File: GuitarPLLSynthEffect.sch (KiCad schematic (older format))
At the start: 36 parts

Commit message: Second draft PCB layout
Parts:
- C_PWRBY1: footprint Capacitors_SMD:C_0805_HandSoldering -> Capacitors_SMD:CP_Elec_4x5.3
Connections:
- net 9V: now also C_PWRBY1.1, C_PWRBY2.2
- net at D_IN1.2 (A), J_POWER1.2: no longer C_PWRBY1.1, C_PWRBY2.2
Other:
- moved on the sheet: C_PWRBY1, C_PWRBY2, D_IN1
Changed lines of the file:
@@
 	1    0    0    1
 $EndComp
-Text Label 2625 2100 3    60   ~ 0
+Text Label 3225 2100 3    60   ~ 0
 GND
 Text Label 4250 1400 0    60   ~ 0
@@
 Wire Wire Line
 	9950 5500 9950 5975
-Wire Wire Line
-	2050 1350 2050 1450
-Connection ~ 2050 1400
+Connection ~ 2650 1400
 Wire Wire Line
 	4075 1400 4075 1600
@@
 Optional clean signal for FX
 Wire Wire Line
-	1475 1400 3125 1400
-Wire Wire Line
-	3425 1400 5350 1400
+	2200 1400 5350 1400
 $Comp
 L _Schottky D_IN1
 U 1 1 5AC34A74
-P 3275 1400
-F 0 "D_IN1" H 3275 1500 50  0000 C CNN
-F 1 "_Schottky" H 3275 1300 50  0000 C CNN
-F 2 "Diodes_SMD:D_SOD-123F" H 3275 1400 50  0001 C CNN
-F 3 "" H 3275 1400 50  0001 C CNN
-	1    3275 1400
+P 2050 1400
+F 0 "D_IN1" H 2050 1500 50  0000 C CNN
+F 1 "_Schottky" H 2050 1300 50  0000 C CNN
+F 2 "Diodes_SMD:D_SOD-123F" H 2050 1400 50  0001 C CNN
+F 3 "" H 2050 1400 50  0001 C CNN
+	1    2050 1400
 	-1   0    0    1
 $EndComp
@@
 	1550 1600 1550 1825
 Wire Wire Line
-	1550 1825 2625 1825
-Wire Wire Line
-	2625 1750 2625 2100
-Wire Wire Line
-	2050 1750 2050 1825
-Connection ~ 2050 1825
+	1550 1825 3225 1825
+Wire Wire Line
+	3225 1750 3225 2100
+Wire Wire Line
+	2650 1750 2650 1825
+Connection ~ 2650 1825
 $Comp
 L C C_PWRBY1
 U 1 1 5AC36CD5
-P 2050 1600
-F 0 "C_PWRBY1" H 2075 1700 50  0000 L CNN
-F 1 "10uF" H 2075 1500 50  0000 L CNN
-F 2 "Capacitors_SMD:C_0805_HandSoldering" H 2088 1450 50  0001 C CNN
-F 3 "" H 2050 1600 50  0001 C CNN
-	1    2050 1600
+P 2650 1600
+F 0 "C_PWRBY1" H 2675 1700 50  0000 L CNN
+F 1 "10uF" H 2675 1500 50  0000 L CNN
+F 2 "Capacitors_SMD:CP_Elec_4x5.3" H 2688 1450 50  0001 C CNN
+F 3 "" H 2650 1600 50  0001 C CNN
+	1    2650 1600
 	1    0    0    -1
 $EndComp
@@
 L PWR_FLAG #FLG01
 U 1 1 5AC38031
-P 2050 1350
-F 0 "#FLG01" H 2050 1425 50  0001 C CNN
-F 1 "PWR_FLAG" H 2050 1500 50  0000 C CNN
-F 2 "" H 2050 1350 50  0001 C CNN
-F 3 "" H 2050 1350 50  0001 C CNN
-	1    2050 1350
+P 1600 1350
+F 0 "#FLG01" H 1600 1425 50  0001 C CNN
+F 1 "PWR_FLAG" H 1600 1500 50  0000 C CNN
+F 2 "" H 1600 1350 50  0001 C CNN
+F 3 "" H 1600 1350 50  0001 C CNN
+	1    1600 1350
 	1    0    0    -1
 $EndComp
@@
 L C C_PWRBY2
 U 1 1 5AC5AF9D
-P 2625 1600
-F 0 "C_PWRBY2" H 2225 1500 50  0000 L CNN
-F 1 "100nF" H 2375 1700 50  0000 L CNN
-F 2 "Capacitors_SMD:C_0805_HandSoldering" H 2663 1450 50  0001 C CNN
-F 3 "" H 2625 1600 50  0001 C CNN
-	1    2625 1600
+P 3225 1600
+F 0 "C_PWRBY2" H 2825 1500 50  0000 L CNN
+F 1 "100nF" H 2975 1700 50  0000 L CNN
+F 2 "Capacitors_SMD:C_0805_HandSoldering" H 3263 1450 50  0001 C CNN
+F 3 "" H 3225 1600 50  0001 C CNN
+	1    3225 1600
 	-1   0    0    1
 $EndComp
 Wire Wire Line
-	2625 1450 2625 1400
-Connection ~ 2625 1400
-Connection ~ 2625 1825
+	3225 1450 3225 1400
+Connection ~ 3225 1400
+Connection ~ 3225 1825
+Wire Wire Line
+	1475 1400 1900 1400
+Wire Wire Line
+	1600 1350 1600 1400
+Connection ~ 1600 1400
+Wire Wire Line
+	2650 1450 2650 1400
 $EndSCHEMATC

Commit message: layout update
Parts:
- removed C_OABY3, C_OABY4, C_OABY5, C_OABY6: 100nF, Capacitors_SMD:C_0805_HandSoldering, symbol C
- removed U_OACLEAN_IN1, U_OA_FXVOL1, U_OA_MIX1: _TL071, SMD_Packages:SOIC-8-N, symbol _TL071
- added U_MAINOA1: TL074, SMD_Packages:SOIC-14_N, symbol TL074
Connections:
- net -9V: now also U_MAINOA1.11 (V-), U_MAINOA1.11 (V-), U_MAINOA1.11 (V-), U_MAINOA1.11 (V-)
- net 9V: now also U_MAINOA1.4 (V+), U_MAINOA1.4 (V+), U_MAINOA1.4 (V+), U_MAINOA1.4 (V+)
- net FXVOL_P1_2: now also U_MAINOA1.6 (-)
- net FXVOL_P3: now also U_MAINOA1.7
- net INSW_P1: now also U_MAINOA1.12 (+)
- net MIX_P3: now also U_MAINOA1.13 (-), U_MAINOA1.14
- net Sheet5AC1BF71/SIG_OUT: now also U_MAINOA1.5 (+)
- net at J_OU1.1 (TIP), R_MIX_F1.1: now also U_MAINOA1.8
- net at R_MIX_F1.2, R_MIX_G1.2: now also U_MAINOA1.9 (-)
- net at SW_BYPASS1.5 (B): now also U_MAINOA1.10 (+)
- no-connect marks 22 -> 19
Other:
- moved on the sheet: C_OABY1, C_OABY2, FXVOL1, J_AUX2MAIN_VOL1, J_MAIN2AUX_VOL1, MIX1

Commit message: update
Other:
- note added: "SPDT\nFX INPUT\nSELECTOR\nON-ON"
- note removed: "SPDT\nFX INPUT\nSELECTOR"
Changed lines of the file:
@@
 NoConn ~ 1750 7475
 Text Notes 3500 4950 0    39   ~ 0
-  SPDT\nFX INPUT\nSELECTOR
+  SPDT\nFX INPUT\nSELECTOR\nON-ON
 Wire Wire Line
 	4700 6850 4375 6850

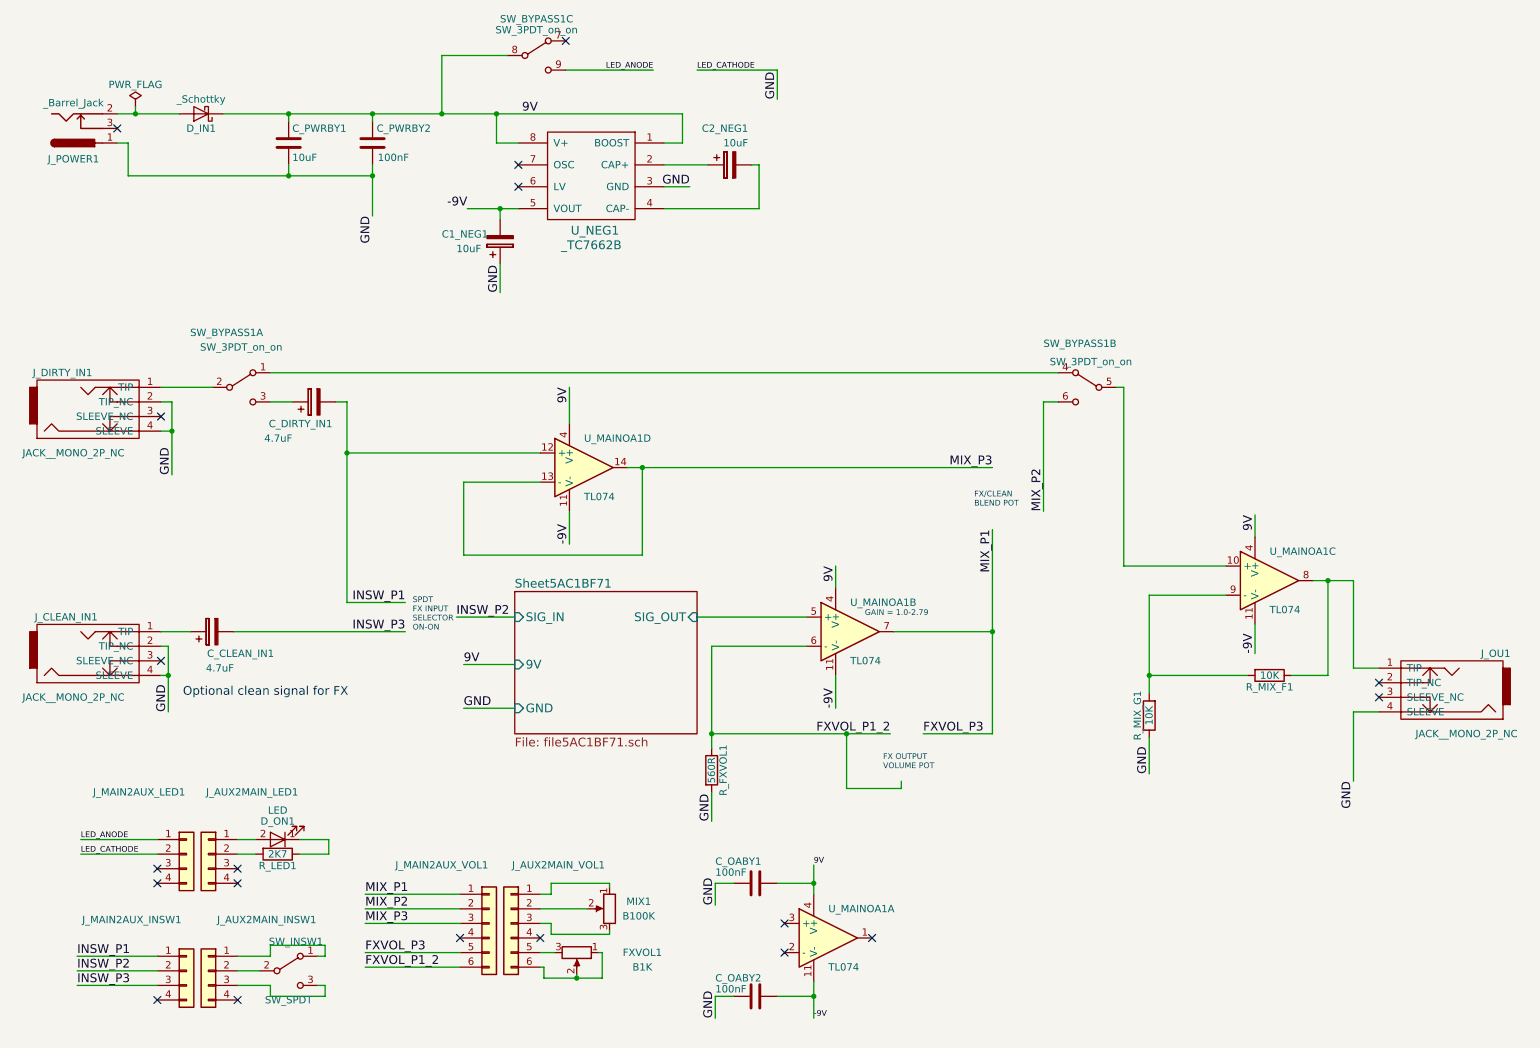
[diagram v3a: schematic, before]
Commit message: Board Redesign - RevB
- Created seperate ground plane for DC-DC Converters
- Re-routed the rest of the board.
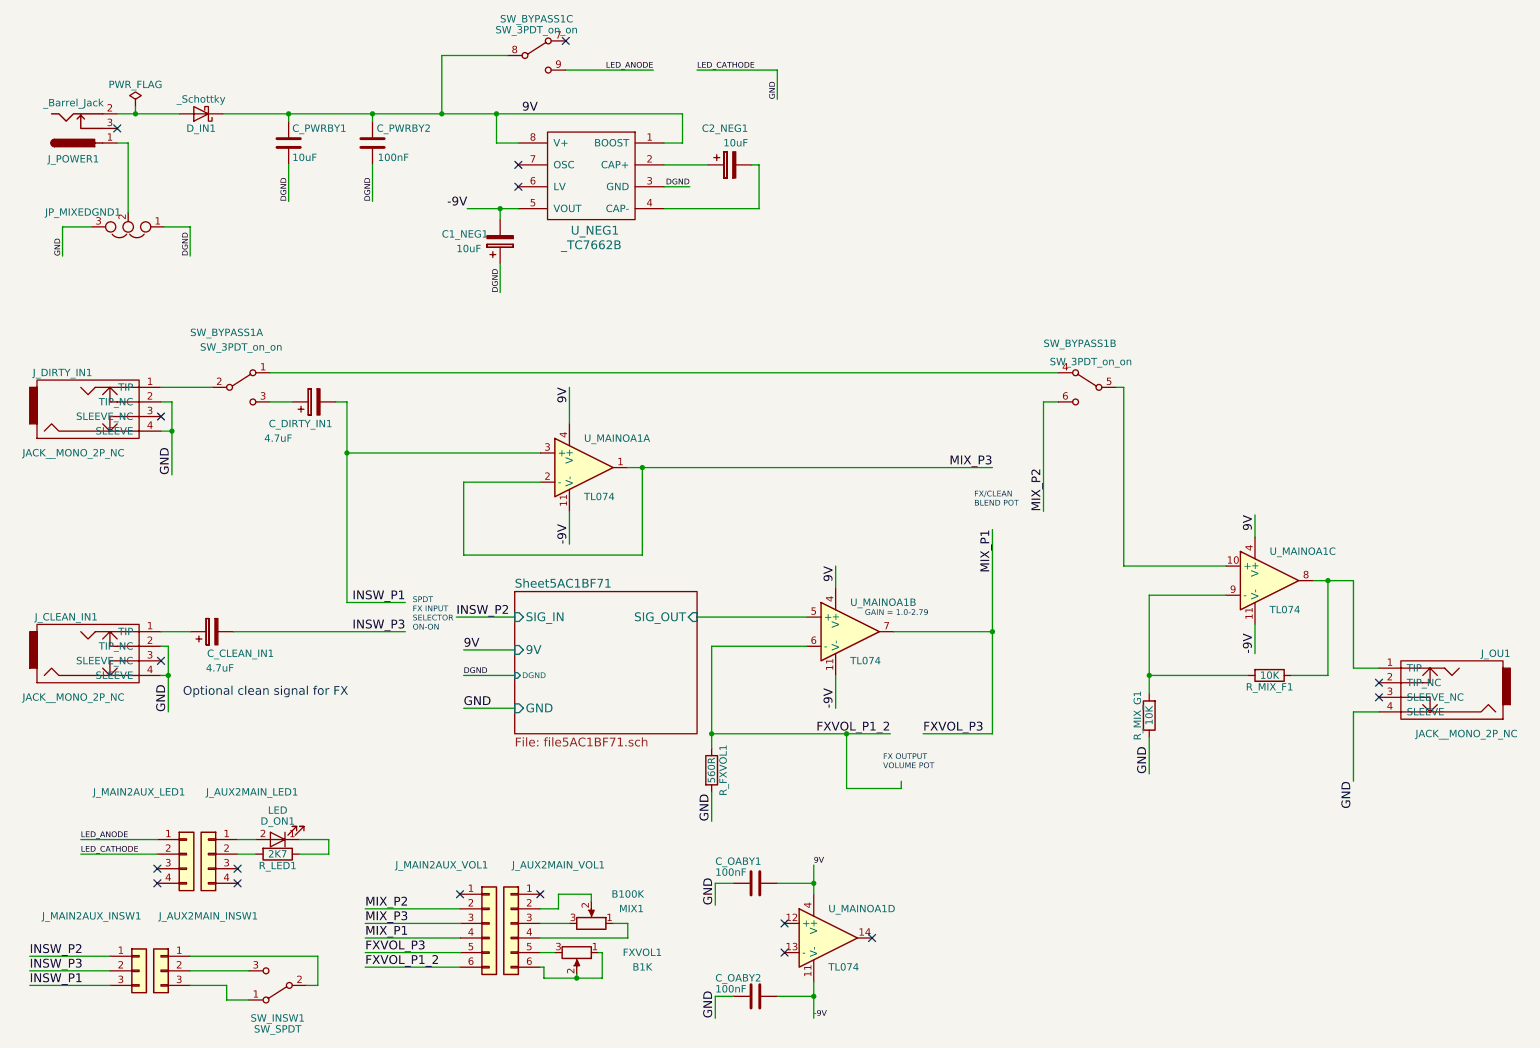
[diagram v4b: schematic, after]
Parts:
- removed J_AUX2MAIN_INSW1, J_MAIN2AUX_INSW1: Conn_01x04, Pin_Headers:Pin_Header_Straight_1x04_Pitch2.54mm, symbol Conn_01x04
- added JP_MIXEDGND1: Jumper_NC_Dual, Oddities:NetTie-II_Connected_SMD, symbol Jumper_NC_Dual
- added J_AUX2MAIN_INSW1, J_MAIN2AUX_INSW1: Conn_01x03, Pin_Headers:Pin_Header_Straight_1x03_Pitch2.54mm, symbol Conn_01x03
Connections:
- net FXVOL_P3: now also J_MAIN2AUX_VOL1.4 (Pin_4); no longer J_MAIN2AUX_VOL1.1 (Pin_1)
- net GND: now also JP_MIXEDGND1.3; no longer C1_NEG1.1, C_PWRBY1.2, C_PWRBY2.1, J_POWER1.1, U_NEG1.3 (GND)
- net INSW_P1: now also U_MAINOA1.3 (+), J_MAIN2AUX_INSW1.3 (Pin_3); no longer U_MAINOA1.12 (+)
- net INSW_P2: now also J_MAIN2AUX_INSW1.1 (Pin_1)
- net INSW_P3: now also J_MAIN2AUX_INSW1.2 (Pin_2)
- net MIX_P3: now also U_MAINOA1.1, U_MAINOA1.2 (-); no longer U_MAINOA1.13 (-), U_MAINOA1.14
- net at MIX1.1: now also J_AUX2MAIN_VOL1.4 (Pin_4); no longer J_AUX2MAIN_VOL1.1 (Pin_1)
- net at SW_INSW1.1 (A): now also J_AUX2MAIN_INSW1.3 (Pin_3)
- net at SW_INSW1.2 (B): now also J_AUX2MAIN_INSW1.1 (Pin_1)
- net at SW_INSW1.3 (C): now also J_AUX2MAIN_INSW1.2 (Pin_2)
- new net: JP_MIXEDGND1.2, J_POWER1.1
- new net DGND: C1_NEG1.1, C_PWRBY1.2, C_PWRBY2.1, JP_MIXEDGND1.1, U_NEG1.3 (GND)
- no-connect marks 19 -> 17
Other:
- moved on the sheet: MIX1, SW_INSW1, U_MAINOA1A, U_MAINOA1D
